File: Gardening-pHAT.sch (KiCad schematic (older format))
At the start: 21 parts, among them P1 CONN_01X03, P2 CONN_01X03, P3 CONN_01X03, P4 CONN_02X05, U1 CAT24C32WI-GT3, U2 MCP3002

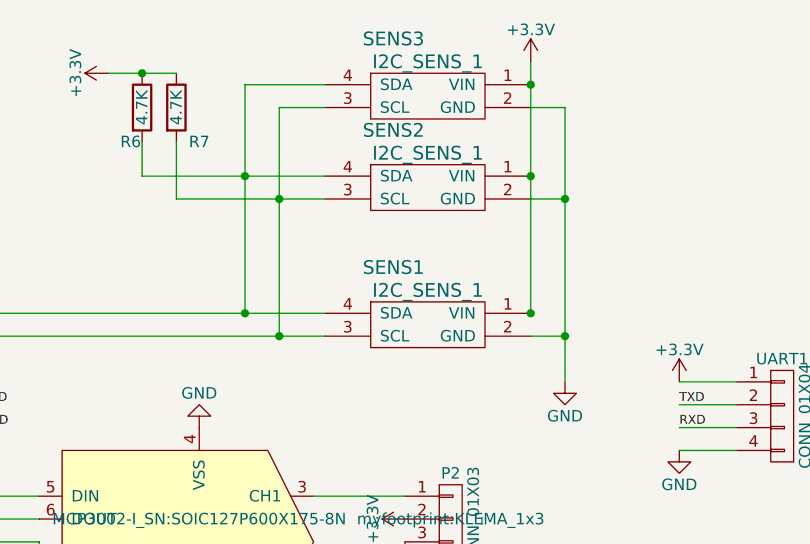
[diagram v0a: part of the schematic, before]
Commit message: Remove one I2C slot and change labels
Leave only two I2C slots to ensure that there is
enough space for the labels. Fix wiring issues.

Signed-off-by: Leon Anavi <leon@anavi.org>
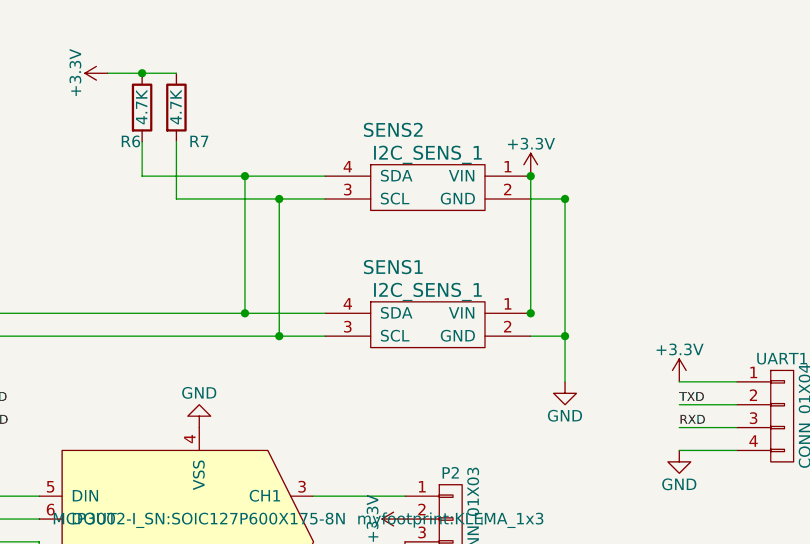
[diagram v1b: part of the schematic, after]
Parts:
- removed SENS3: I2C_SENS_1, Pin_Headers:Pin_Header_Straight_1x04, symbol I2C_SENS_1
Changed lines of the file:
@@
 L +3.3V #PWR18
 U 1 1 5704BA43
-P 7900 700
-F 0 "#PWR18" H 7900 550 50  0001 C CNN
-F 1 "+3.3V" H 7900 840 50  0000 C CNN
-F 2 "" H 7900 700 50  0000 C CNN
-F 3 "" H 7900 700 50  0000 C CNN
-	1    7900 700
+P 7900 1200
+F 0 "#PWR18" H 7900 1050 50  0001 C CNN
+F 1 "+3.3V" H 7900 1340 50  0000 C CNN
+F 2 "" H 7900 1200 50  0000 C CNN
+F 3 "" H 7900 1200 50  0000 C CNN
+	1    7900 1200
 	1    0    0    -1
 $EndComp
@@
 F 3 "" H 7200 1100 60  0000 C CNN
 	1    7200 1100
-	1    0    0    -1
-$EndComp
-$Comp
-L I2C_SENS_1 SENS3
-U 1 1 5752A2F7
-P 7200 700
-F 0 "SENS3" H 7300 800 60  0000 C CNN
-F 1 "I2C_SENS_1" H 7450 700 60  0000 C CNN
-F 2 "Pin_Headers:Pin_Header_Straight_1x04" H 7200 700 60  0001 C CNN
-F 3 "" H 7200 700 60  0000 C CNN
-	1    7200 700
 	1    0    0    -1
 $EndComp
@@
 	0    -1   -1   0
 $EndComp
-Wire Wire Line
-	950  3500 800  3500
-Wire Wire Line
-	800  3500 800  3950
-Wire Wire Line
-	950  3600 800  3600
-Connection ~ 800  3600
-Wire Wire Line
-	950  3700 800  3700
-Connection ~ 800  3700
-Wire Wire Line
-	950  3800 800  3800
-Connection ~ 800  3800
-Wire Wire Line
-	2200 3500 2050 3500
-Connection ~ 2200 3050
-Wire Wire Line
-	2950 3050 2950 3200
-Wire Wire Line
-	2800 3050 2800 3200
-Connection ~ 2800 3050
-Wire Wire Line
-	2650 3200 2650 3050
-Connection ~ 2650 3050
-Wire Wire Line
-	2200 3050 2950 3050
-Wire Wire Line
-	2050 3600 2650 3600
-Wire Wire Line
-	2650 3500 2650 4050
-Wire Wire Line
-	2800 3700 2800 3500
-Wire Wire Line
-	2950 3800 2950 3500
-Connection ~ 2950 3800
-Connection ~ 2800 3700
-Wire Wire Line
-	2200 2700 2200 3500
-Connection ~ 2650 3600
-Wire Wire Line
-	3450 2150 3450 2250
-Connection ~ 3450 2150
-Connection ~ 3450 1800
-Wire Wire Line
-	3450 1800 3450 1900
-Wire Wire Line
-	5350 1800 7000 1800
-Wire Wire Line
-	5350 1900 7000 1900
-Connection ~ 6650 1800
-Connection ~ 6800 1900
-Wire Wire Line
-	8050 900  8050 2100
-Wire Wire Line
-	8050 1900 7900 1900
-Connection ~ 7900 1800
-Wire Wire Line
-	2050 3700 3450 3700
-Wire Wire Line
-	2050 3800 3450 3800
-Wire Wire Line
-	8800 2400 8550 2400
-Wire Wire Line
-	8550 2100 8800 2100
-Wire Wire Line
-	5350 2200 5500 2200
-Wire Wire Line
-	5350 2300 5500 2300
-Wire Wire Line
-	8800 2200 8550 2200
-Wire Wire Line
-	8800 2300 8550 2300
-Connection ~ 7900 1200
-Connection ~ 7900 800
-Wire Wire Line
-	7900 900  8050 900
-Wire Wire Line
-	8050 1300 7900 1300
-Connection ~ 8050 1900
-Connection ~ 8050 1300
-Wire Wire Line
-	7000 800  6650 800
-Wire Wire Line
-	6200 1200 7000 1200
-Connection ~ 6650 1200
-Wire Wire Line
-	7000 900  6800 900
-Wire Wire Line
-	6350 1300 7000 1300
-Connection ~ 6800 1300
-Wire Wire Line
-	6350 1050 6350 1300
-Wire Wire Line
-	6200 1050 6200 1200
-Wire Wire Line
-	6050 750  6350 750
-Connection ~ 6200 750
-Wire Wire Line
-	6800 900  6800 1900
-Wire Wire Line
-	6650 800  6650 1800
-Wire Wire Line
-	7900 700  7900 1800
-Wire Wire Line
-	3450 2650 3450 3450
-Connection ~ 3450 2750
-Connection ~ 3450 2850
-Connection ~ 3450 2950
-Connection ~ 3450 3050
-Connection ~ 3450 3150
-Connection ~ 3450 3350
-Connection ~ 3450 3250
-Wire Wire Line
-	6950 3000 7350 3000
-Wire Wire Line
-	6950 2600 7350 2600
-Wire Wire Line
-	6400 3650 6800 3650
-Wire Wire Line
-	5350 3450 6100 3450
-Wire Wire Line
-	5750 2600 5350 2600
-Wire Wire Line
-	5350 2700 5750 2700
-Wire Wire Line
-	5350 2800 5750 2800
-Wire Wire Line
-	5750 2800 5750 2900
-Wire Wire Line
-	5350 2900 5650 2900
-Wire Wire Line
-	5650 2900 5650 3000
-Wire Wire Line
-	5650 3000 5750 3000
 $Comp
 L CONN_02X05 P4
@@
 	0    -1   -1   0
 $EndComp
-Wire Wire Line
-	5350 4150 8100 4150
-Wire Wire Line
-	8100 4150 8100 3950
-Wire Wire Line
-	5350 4050 8200 4050
-Wire Wire Line
-	8200 4050 8200 3950
-Wire Wire Line
-	5350 5050 8300 5050
-Wire Wire Line
-	8300 5050 8300 3950
 $Comp
 L GND #PWR20
@@
 $EndComp
 Wire Wire Line
+	950  3500 800  3500
+Wire Wire Line
+	800  3500 800  3950
+Wire Wire Line
+	950  3600 800  3600
+Connection ~ 800  3600
+Wire Wire Line
+	950  3700 800  3700
+Connection ~ 800  3700
+Wire Wire Line
+	950  3800 800  3800
+Connection ~ 800  3800
+Wire Wire Line
+	2200 3500 2050 3500
+Connection ~ 2200 3050
+Wire Wire Line
+	2950 3050 2950 3200
+Wire Wire Line
+	2800 3050 2800 3200
+Connection ~ 2800 3050
+Wire Wire Line
+	2650 3200 2650 3050
+Connection ~ 2650 3050
+Wire Wire Line
+	2200 3050 2950 3050
+Wire Wire Line
+	2050 3600 2650 3600
+Wire Wire Line
+	2650 3500 2650 4050
+Wire Wire Line
+	2800 3700 2800 3500
+Wire Wire Line
+	2950 3800 2950 3500
+Connection ~ 2950 3800
+Connection ~ 2800 3700
+Wire Wire Line
+	2200 2700 2200 3500
+Connection ~ 2650 3600
+Wire Wire Line
+	3450 2150 3450 2250
+Connection ~ 3450 2150
+Connection ~ 3450 1800
+Wire Wire Line
+	3450 1800 3450 1900
+Wire Wire Line
+	5350 1800 7000 1800
+Wire Wire Line
+	5350 1900 7000 1900
+Connection ~ 6650 1800
+Connection ~ 6800 1900
+Wire Wire Line
+	8050 1900 7900 1900
+Connection ~ 7900 1800
+Wire Wire Line
+	2050 3700 3450 3700
+Wire Wire Line
+	2050 3800 3450 3800
+Wire Wire Line
+	8800 2400 8550 2400
+Wire Wire Line
+	8550 2100 8800 2100
+Wire Wire Line
+	5350 2200 5500 2200
+Wire Wire Line
+	5350 2300 5500 2300
+Wire Wire Line
+	8800 2200 8550 2200
+Wire Wire Line
+	8800 2300 8550 2300
+Connection ~ 7900 1200
+Wire Wire Line
+	8050 1300 7900 1300
+Connection ~ 8050 1900
+Connection ~ 8050 1300
+Wire Wire Line
+	6200 1200 7000 1200
+Connection ~ 6650 1200
+Wire Wire Line
+	6350 1300 7000 1300
+Connection ~ 6800 1300
+Wire Wire Line
+	6350 1050 6350 1300
+Wire Wire Line
+	6200 1050 6200 1200
+Wire Wire Line
+	6050 750  6350 750
+Connection ~ 6200 750
+Wire Wire Line
+	3450 2650 3450 3450
+Connection ~ 3450 2750
+Connection ~ 3450 2850
+Connection ~ 3450 2950
+Connection ~ 3450 3050
+Connection ~ 3450 3150
+Connection ~ 3450 3350
+Connection ~ 3450 3250
+Wire Wire Line
+	6950 3000 7350 3000
+Wire Wire Line
+	6950 2600 7350 2600
+Wire Wire Line
+	6400 3650 6800 3650
+Wire Wire Line
+	5350 3450 6100 3450
+Wire Wire Line
+	5750 2600 5350 2600
+Wire Wire Line
+	5350 2700 5750 2700
+Wire Wire Line
+	5350 2800 5750 2800
+Wire Wire Line
+	5750 2800 5750 2900
+Wire Wire Line
+	5350 2900 5650 2900
+Wire Wire Line
+	5650 2900 5650 3000
+Wire Wire Line
+	5650 3000 5750 3000
+Wire Wire Line
+	5350 4150 8100 4150
+Wire Wire Line
+	8100 4150 8100 3950
+Wire Wire Line
+	5350 4050 8200 4050
+Wire Wire Line
+	8200 4050 8200 3950
+Wire Wire Line
+	5350 5050 8300 5050
+Wire Wire Line
+	8300 5050 8300 3950
+Wire Wire Line
 	6100 3450 6100 3650
+Wire Wire Line
+	6650 1800 6650 1200
+Wire Wire Line
+	6800 1900 6800 1300
+Wire Wire Line
+	8050 1300 8050 2100
+Wire Wire Line
+	7900 1800 7900 1200
 $EndSCHEMATC
